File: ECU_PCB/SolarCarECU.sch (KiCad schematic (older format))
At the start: 181 parts, among them J2 Screw_Terminal_01x08, J3 Screw_Terminal_01x08, J4 Screw_Terminal_01x08, J5 Screw_Terminal_01x08, J6 Screw_Terminal_01x08, J7 Screw_Terminal_01x08, J8 Screw_Terminal_01x08, Q1 QM6015D, Q2 QM6015D, Q3 QM6015D, Q4 QM6015D, Q5 QM6015D, Q6 QM6015D, Q7 QM6015D, U1 Teensy3.6, U10 LM324A, U11 MCP1403, U2 MCP1403, U3 MCP1403, U4 L7805, U5 MCP2562-E-P, U6 MCP2562-E-P, U7 4504, U8 4504, U9 4504

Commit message: finished PCB (but forgot to save so commiting again)
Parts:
- R29, R31, R40, R43, R44, R45, R46, R47, R48, R49, R50, R51, R54, R55, R56, R60, R61, R62, R63: renamed from R?; footprint Resistor_SMD:R_1206_3216Metric -> Resistor_SMD:R_0603_1608Metric
- gave numbers to parts that had none: 76

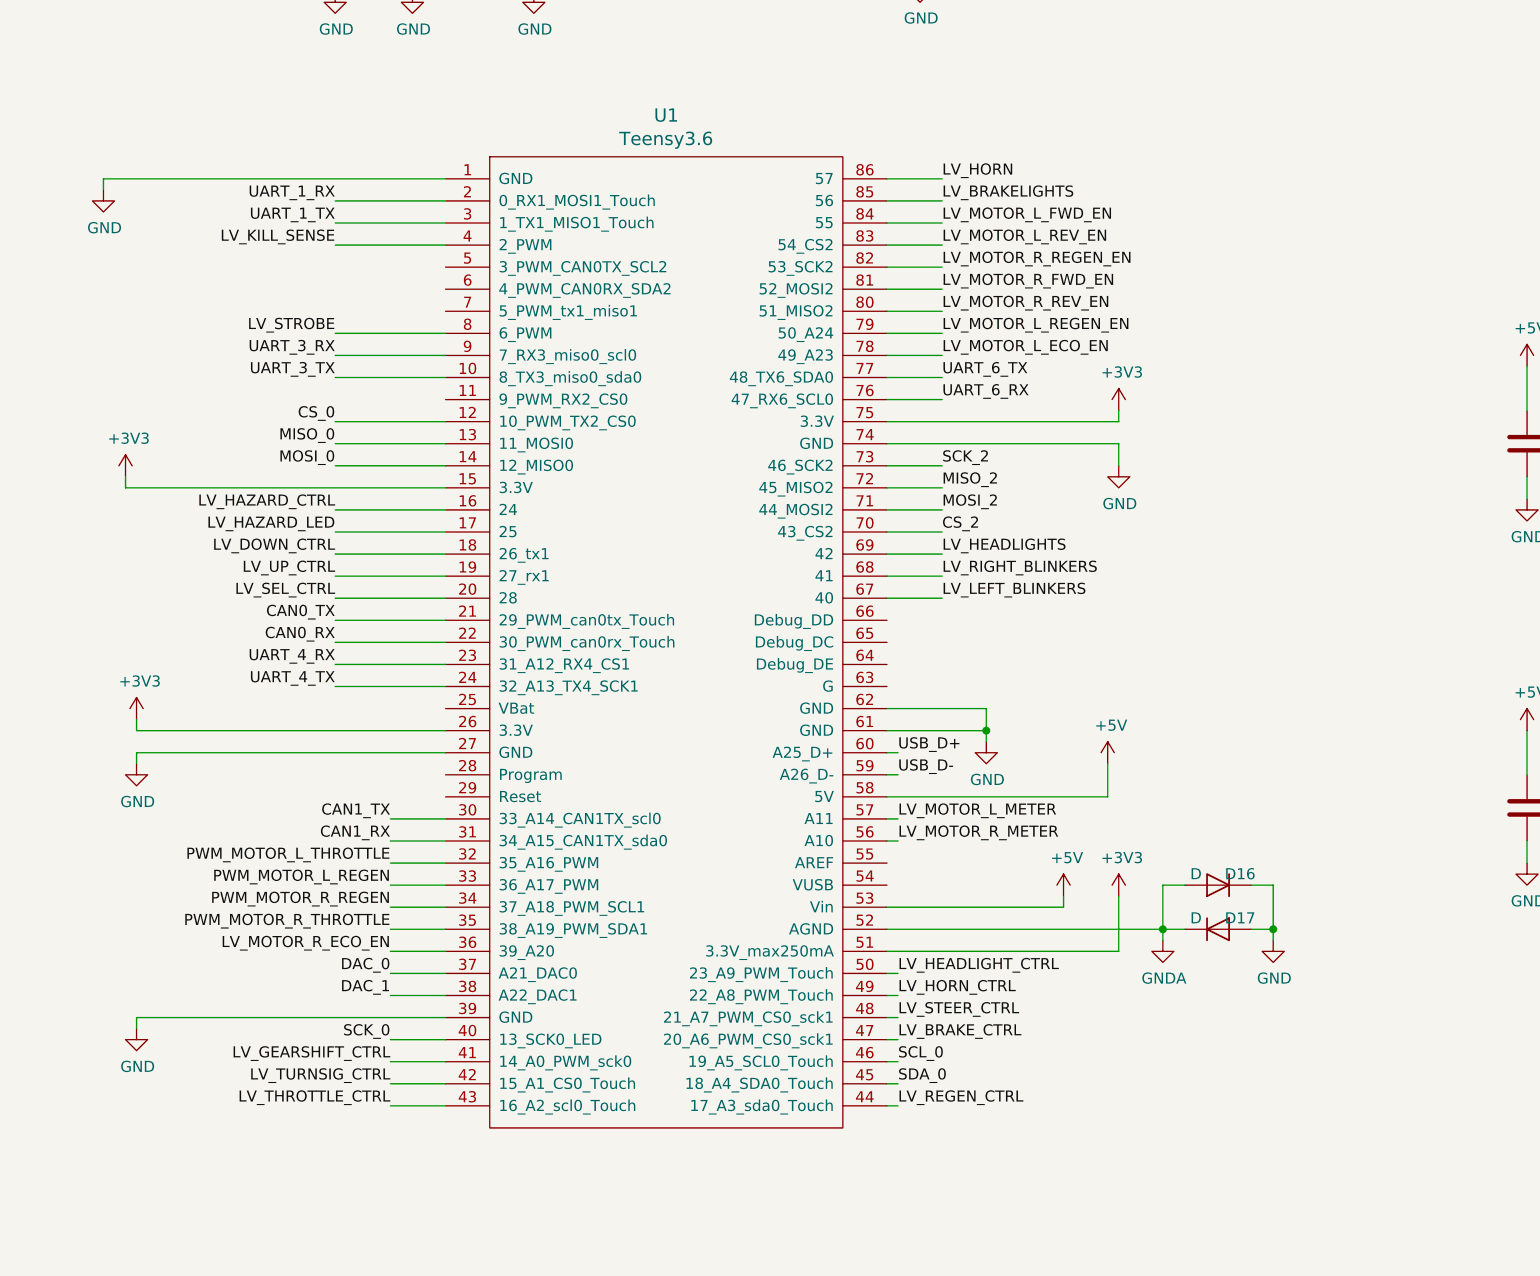
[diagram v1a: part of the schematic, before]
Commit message: added PTC fuses to all teensy inputs. PCB not modified to match new PCB.
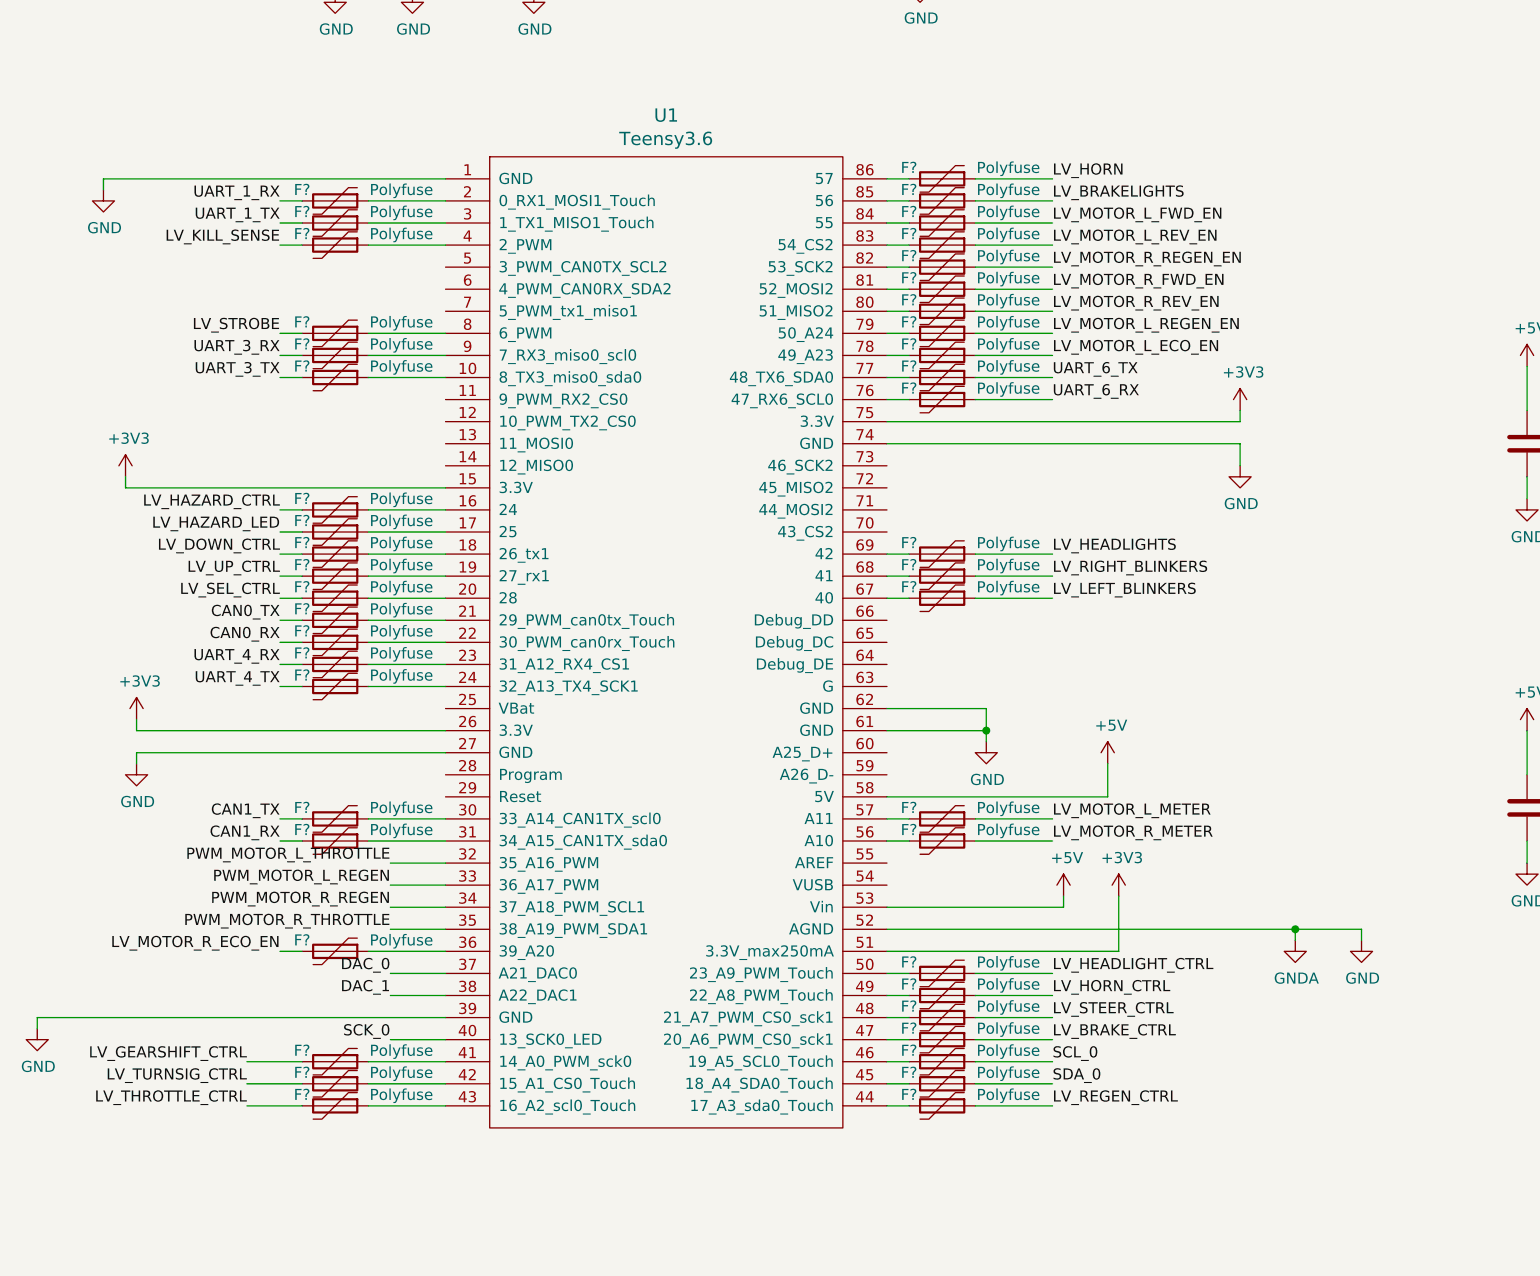
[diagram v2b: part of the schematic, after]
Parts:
- removed D16, D17: D, Diode_SMD:D_SOD-123, symbol Device:D
- added F? (x44): Polyfuse, symbol Device:Polyfuse
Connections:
- net GNDA is gone; now on net GND: C22.2, C23.2, C24.2, C25.2, C31.1, C32.1, C33.1, C34.1, C35.2, C36.2, C37.2, C38.2, C39.2, C40.2, C41.2, C42.2, C43.1, C44.2, J3.8 (Pin_8), J4.8 (Pin_8), J5.2 (Pin_2), J6.1 (Pin_1), R33.2, R35.2, R37.2, R39.2, R59.2, R60.2, R61.2, R62.2, R63.2, R66.2, R69.2, R72.2, R74.2, R77.2, R80.2, R83.2, R86.2, U1.52 (AGND)
- net CAN0_RX: now also F?.2; no longer U1.22 (30_PWM_can0rx_Touch)
- net CAN0_TX: now also F?.2; no longer U1.21 (29_PWM_can0tx_Touch)
- net CAN1_RX: now also F?.2; no longer U1.31 (34_A15_CAN1TX_sda0)
- net CAN1_TX: now also F?.2; no longer U1.30 (33_A14_CAN1TX_scl0)
- net LV_BRAKELIGHTS: now also F?.1; no longer U1.85 (56)
- net LV_BRAKE_CTRL: now also F?.1; no longer U1.47 (20_A6_PWM_CS0_sck1)
- net LV_DOWN_CTRL: now also F?.2; no longer U1.18 (26_tx1)
- net LV_GEARSHIFT_CTRL: now also F?.2; no longer U1.41 (14_A0_PWM_sck0)
- net LV_HAZARD_CTRL: now also F?.2; no longer U1.16 (24)
- net LV_HAZARD_LED: now also F?.2; no longer U1.17 (25)
- net LV_HEADLIGHTS: now also F?.1; no longer U1.69 (42)
- net LV_HEADLIGHT_CTRL: now also F?.1; no longer U1.50 (23_A9_PWM_Touch)
- net LV_HORN: now also F?.1; no longer U1.86 (57)
- net LV_HORN_CTRL: now also F?.1; no longer U1.49 (22_A8_PWM_Touch)
- net LV_KILL_SENSE: now also F?.2; no longer U1.4 (2_PWM)
- net LV_LEFT_BLINKERS: now also F?.1; no longer U1.67 (40)
- net LV_MOTOR_L_ECO_EN: now also F?.1; no longer U1.78 (49_A23)
- net LV_MOTOR_L_FWD_EN: now also F?.1; no longer U1.84 (55)
- net LV_MOTOR_L_METER: now also F?.1; no longer U1.57 (A11)
- net LV_MOTOR_L_REGEN_EN: now also F?.1; no longer U1.79 (50_A24)
- net LV_MOTOR_L_REV_EN: now also F?.1; no longer U1.83 (54_CS2)
- net LV_MOTOR_R_ECO_EN: now also F?.2; no longer U1.36 (39_A20)
- net LV_MOTOR_R_FWD_EN: now also F?.1; no longer U1.81 (52_MOSI2)
- net LV_MOTOR_R_METER: now also F?.1; no longer U1.56 (A10)
- net LV_MOTOR_R_REGEN_EN: now also F?.1; no longer U1.82 (53_SCK2)
- net LV_MOTOR_R_REV_EN: now also F?.1; no longer U1.80 (51_MISO2)
- net LV_REGEN_CTRL: now also F?.1; no longer U1.44 (17_A3_sda0_Touch)
- net LV_RIGHT_BLINKERS: now also F?.1; no longer U1.68 (41)
- net LV_SEL_CTRL: now also F?.2; no longer U1.20 (28)
- net LV_STEER_CTRL: now also F?.1; no longer U1.48 (21_A7_PWM_CS0_sck1)
- net LV_STROBE: now also F?.2; no longer U1.8 (6_PWM)
- net LV_THROTTLE_CTRL: now also F?.2; no longer U1.43 (16_A2_scl0_Touch)
- net LV_TURNSIG_CTRL: now also F?.2; no longer U1.42 (15_A1_CS0_Touch)
- net LV_UP_CTRL: now also F?.2; no longer U1.19 (27_rx1)
- net SCL_0: now also F?.1; no longer U1.46 (19_A5_SCL0_Touch)
- net SDA_0: now also F?.1; no longer U1.45 (18_A4_SDA0_Touch)
- net UART_1_RX: now also F?.2; no longer U1.2 (0_RX1_MOSI1_Touch)
- net UART_1_TX: now also F?.2; no longer U1.3 (1_TX1_MISO1_Touch)
- net UART_3_RX: now also F?.2; no longer U1.9 (7_RX3_miso0_scl0)
- net UART_3_TX: now also F?.2; no longer U1.10 (8_TX3_miso0_sda0)
- net UART_4_RX: now also F?.2; no longer U1.23 (31_A12_RX4_CS1)
- net UART_4_TX: now also F?.2; no longer U1.24 (32_A13_TX4_SCK1)
- net UART_6_RX: now also F?.1; no longer U1.76 (47_RX6_SCL0)
- net UART_6_TX: now also F?.1; no longer U1.77 (48_TX6_SDA0)
- net CS_0: no longer names the net of U1.12 (10_PWM_TX2_CS0)
- net CS_2: no longer names the net of U1.70 (43_CS2)
- net MISO_0: no longer names the net of U1.13 (11_MOSI0)
- net MISO_2: no longer names the net of U1.72 (45_MISO2)
- net MOSI_0: no longer names the net of U1.14 (12_MISO0)
- net MOSI_2: no longer names the net of U1.71 (44_MOSI2)
- net SCK_2: no longer names the net of U1.73 (46_SCK2)
- net USB_D+: no longer names the net of U1.60 (A25_D+)
- net USB_D-: no longer names the net of U1.59 (A26_D-)
- new net: F?.1, U1.10 (8_TX3_miso0_sda0)
- new net: F?.1, U1.16 (24)
- new net: F?.1, U1.17 (25)
- new net: F?.1, U1.18 (26_tx1)
- new net: F?.1, U1.19 (27_rx1)
- new net: F?.1, U1.2 (0_RX1_MOSI1_Touch)
- new net: F?.1, U1.20 (28)
- new net: F?.1, U1.21 (29_PWM_can0tx_Touch)
- new net: F?.1, U1.22 (30_PWM_can0rx_Touch)
- new net: F?.1, U1.23 (31_A12_RX4_CS1)
- new net: F?.1, U1.24 (32_A13_TX4_SCK1)
- new net: F?.1, U1.3 (1_TX1_MISO1_Touch)
- new net: F?.1, U1.30 (33_A14_CAN1TX_scl0)
- new net: F?.1, U1.31 (34_A15_CAN1TX_sda0)
- new net: F?.1, U1.36 (39_A20)
- new net: F?.1, U1.4 (2_PWM)
- new net: F?.1, U1.41 (14_A0_PWM_sck0)
- new net: F?.1, U1.42 (15_A1_CS0_Touch)
- new net: F?.1, U1.43 (16_A2_scl0_Touch)
- new net: F?.2, U1.44 (17_A3_sda0_Touch)
- new net: F?.2, U1.45 (18_A4_SDA0_Touch)
- new net: F?.2, U1.46 (19_A5_SCL0_Touch)
- new net: F?.2, U1.47 (20_A6_PWM_CS0_sck1)
- new net: F?.2, U1.48 (21_A7_PWM_CS0_sck1)
- new net: F?.2, U1.49 (22_A8_PWM_Touch)
- new net: F?.2, U1.50 (23_A9_PWM_Touch)
- new net: F?.2, U1.56 (A10)
- new net: F?.2, U1.57 (A11)
- new net: F?.2, U1.67 (40)
- new net: F?.2, U1.68 (41)
- new net: F?.2, U1.69 (42)
- new net: F?.2, U1.76 (47_RX6_SCL0)
- new net: F?.2, U1.77 (48_TX6_SDA0)
- new net: F?.2, U1.78 (49_A23)
- new net: F?.2, U1.79 (50_A24)
- new net: F?.1, U1.8 (6_PWM)
- new net: F?.2, U1.80 (51_MISO2)
- new net: F?.2, U1.81 (52_MOSI2)
- new net: F?.2, U1.82 (53_SCK2)
- new net: F?.2, U1.83 (54_CS2)
- new net: F?.2, U1.84 (55)
- new net: F?.2, U1.85 (56)
- new net: F?.2, U1.86 (57)
- new net: F?.1, U1.9 (7_RX3_miso0_scl0)

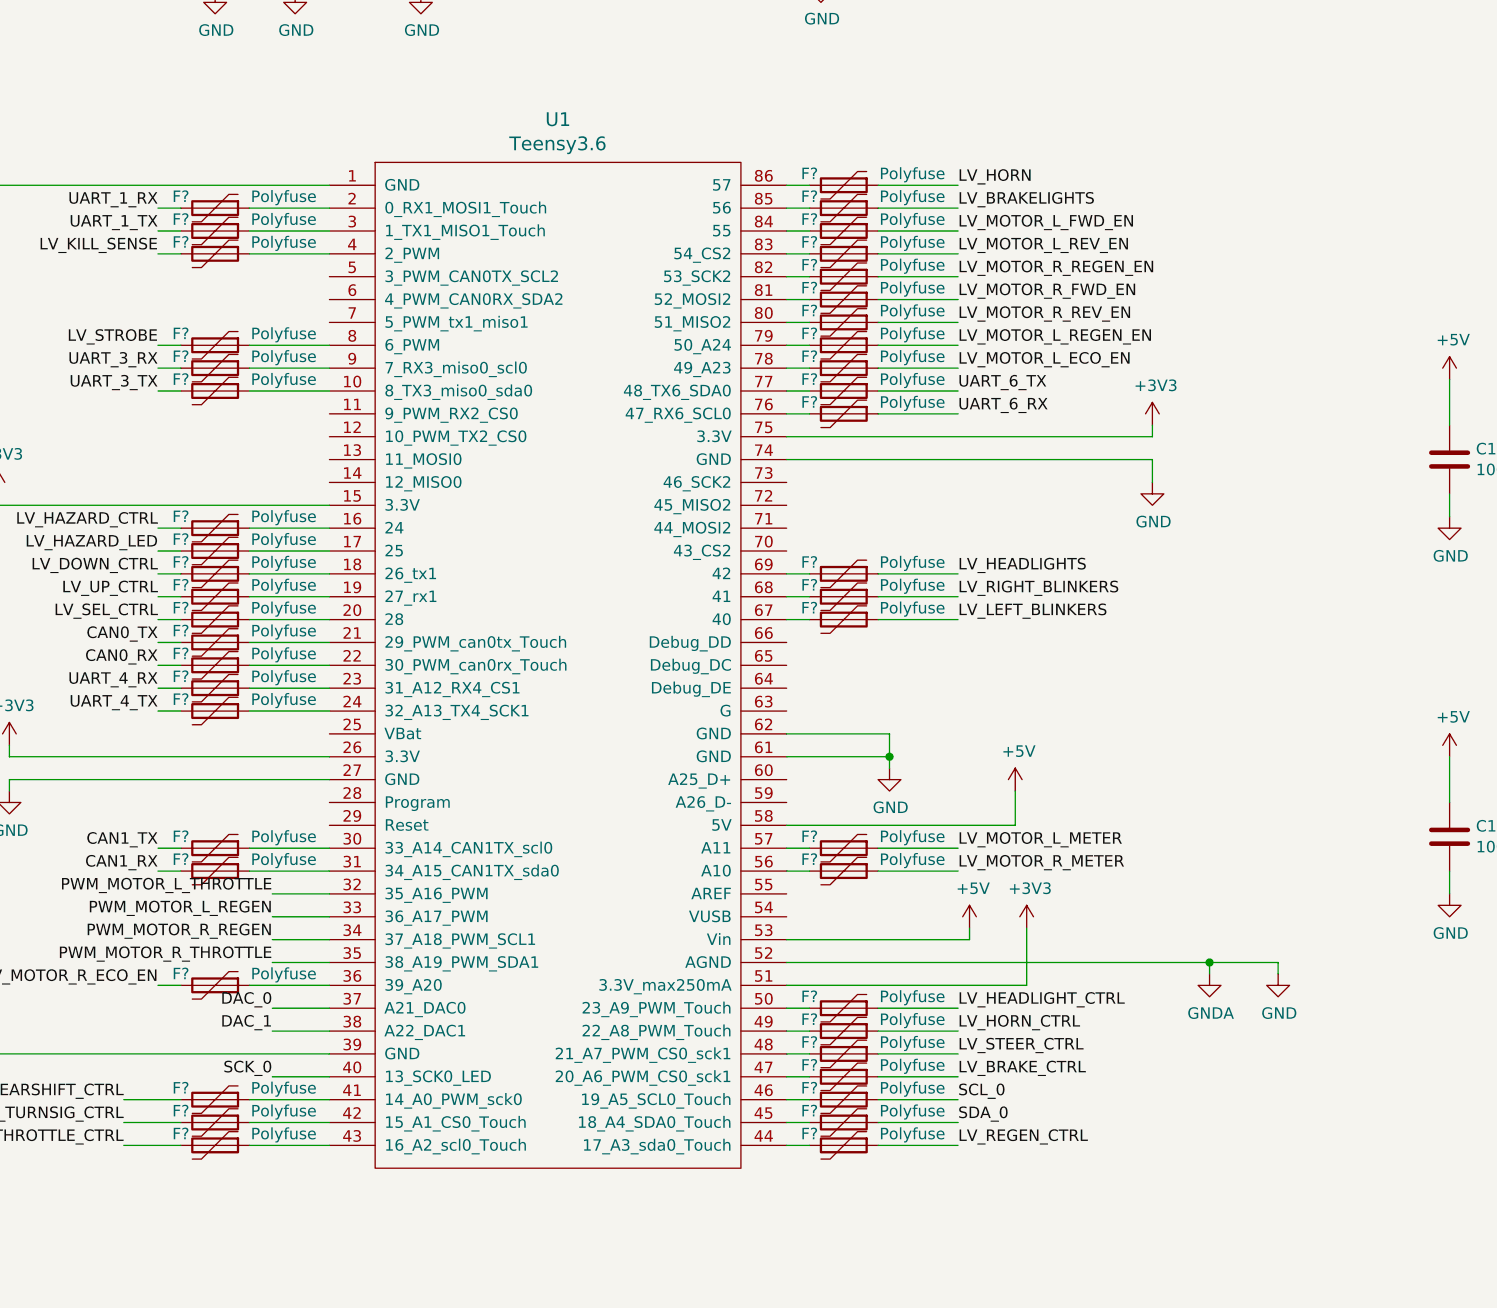
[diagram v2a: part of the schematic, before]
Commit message: added fuse footprints, added 0 ohm resistor to keep gnd/gnda labels consistent, need to update netlist in pcbnew
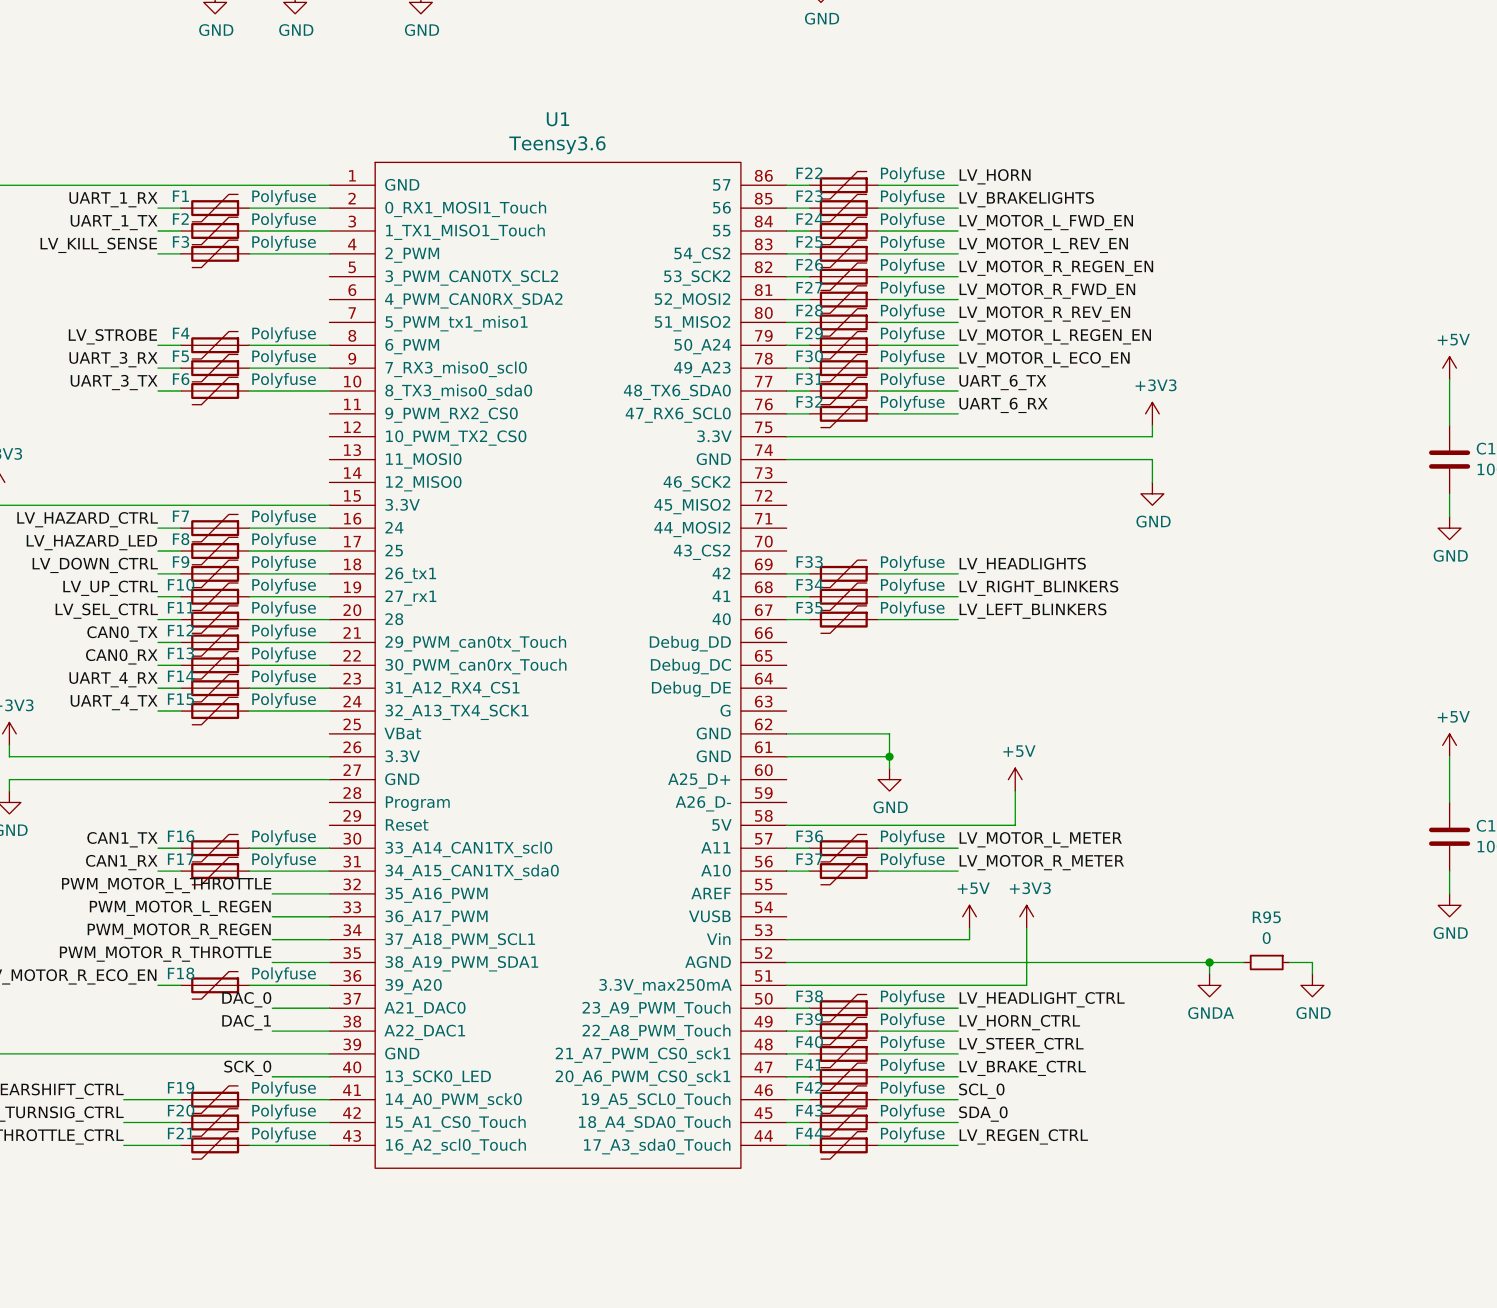
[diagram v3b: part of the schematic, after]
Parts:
- added R95: 0, Resistor_SMD:R_0603_1608Metric, symbol Device:R_Small
- F1, F10, F11, F12, F13, F14, F15, F16, F17, F18, F19, F2, F20, F21, F22, F23, F24, F25, F26, F27, F28, F29, F3, F30, F31, F32, F33, F34, F35, F36, F37, F38, F39, F4, F40, F41, F42, F43, F44, F5, F6, F7, F8, F9: renamed from F?; footprint (none) -> Fuse:Fuse_0603_1608Metric
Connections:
- net GND: now also R95.1; no longer C22.2, C23.2, C24.2, C25.2, C31.1, C32.1, C33.1, C34.1, C35.2, C36.2, C37.2, C38.2, C39.2, C40.2, C41.2, C42.2, C43.1, C44.2, J3.8 (Pin_8), J4.8 (Pin_8), J5.2 (Pin_2), J6.1 (Pin_1), R33.2, R35.2, R37.2, R39.2, R59.2, R60.2, R61.2, R62.2, R63.2, R66.2, R69.2, R72.2, R74.2, R77.2, R80.2, R83.2, R86.2, U1.52 (AGND)
- new net GNDA: C22.2, C23.2, C24.2, C25.2, C31.1, C32.1, C33.1, C34.1, C35.2, C36.2, C37.2, C38.2, C39.2, C40.2, C41.2, C42.2, C43.1, C44.2, J3.8 (Pin_8), J4.8 (Pin_8), J5.2 (Pin_2), J6.1 (Pin_1), R33.2, R35.2, R37.2, R39.2, R59.2, R60.2, R61.2, R62.2, R63.2, R66.2, R69.2, R72.2, R74.2, R77.2, R80.2, R83.2, R86.2, R95.2, U1.52 (AGND)
